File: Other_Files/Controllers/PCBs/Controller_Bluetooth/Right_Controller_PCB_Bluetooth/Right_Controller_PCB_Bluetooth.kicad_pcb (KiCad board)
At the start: 2 copper layers, 53 x 102 mm, 13 parts, among them X1 SW_Push, Y1 SW_Push

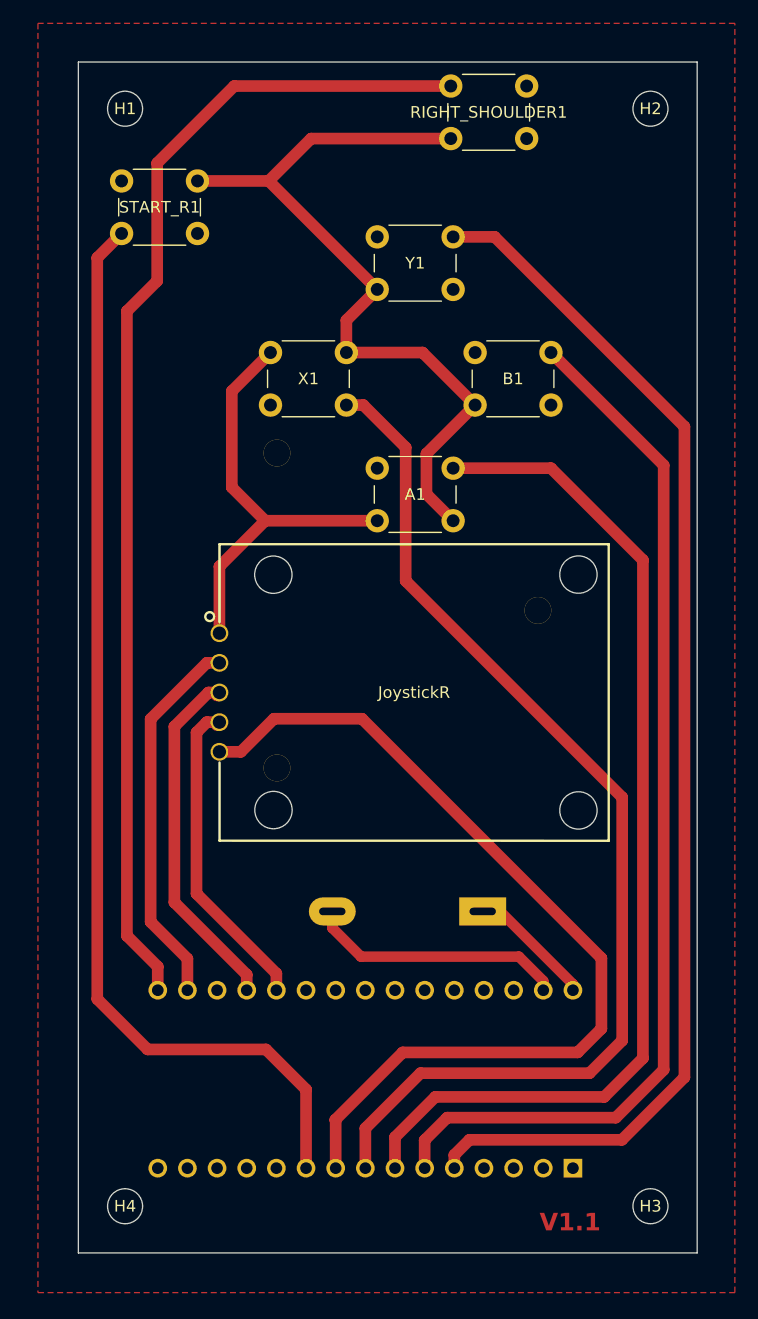
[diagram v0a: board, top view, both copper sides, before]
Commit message: Updated the Controllers' PCB to version 1.2
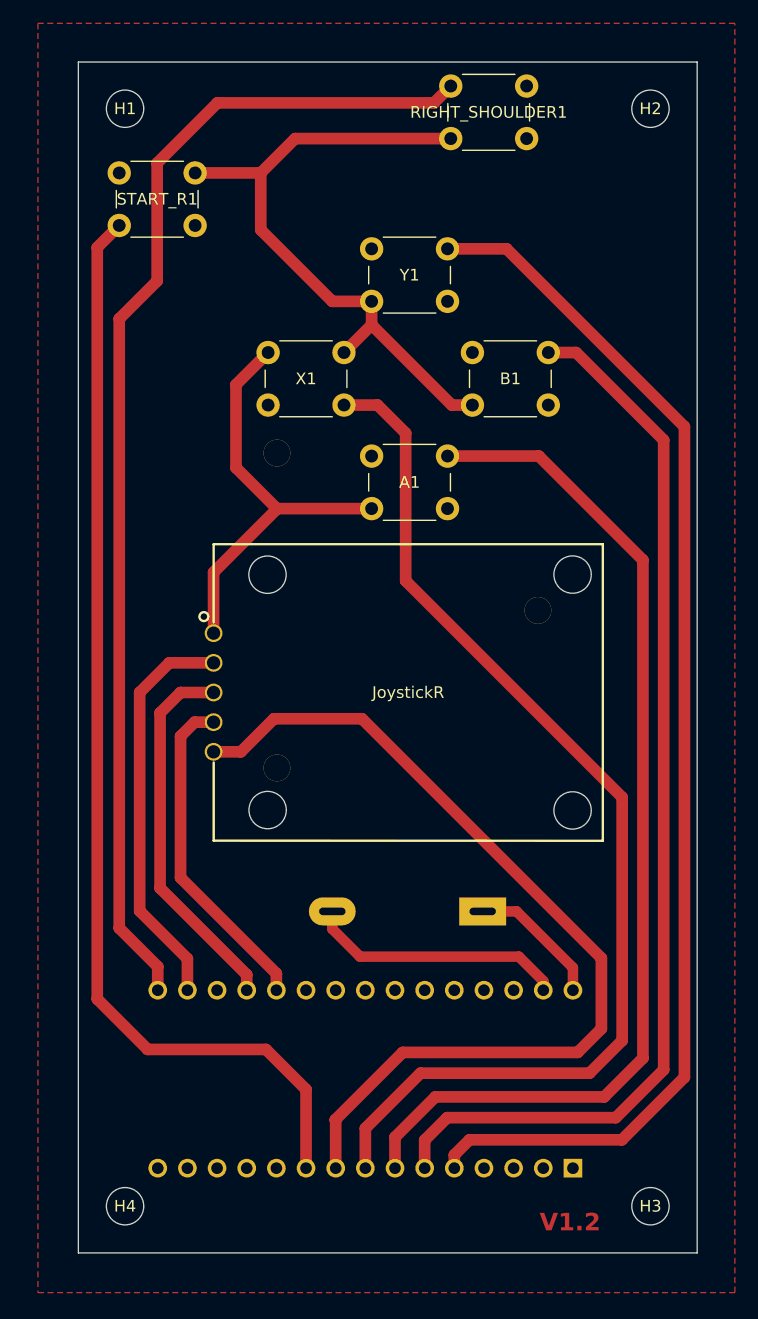
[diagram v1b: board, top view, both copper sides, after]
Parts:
- H1, H2, H3, H4: footprint MountingHole:MountingHole_3mm -> MountingHole:MountingHole_3.2mm_M3
- moved A1 1.14 mm to (142.1, 80.8)
- moved Y1 1.13 mm to (142.1, 63.0)
- moved START_R1 0.72 mm to (127.0, 61.0)
- moved JoystickR1 0.50 mm to (145.2, 101.0)
- moved B1 0.23 mm to (150.8, 71.9)
- moved X1 0.20 mm to (133.2, 71.9)
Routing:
- net GND: track 128.5 -> 116.3 mm
- net +3.3V: track 32.4 -> 34.6 mm
- net /Analog_X_R: track 30.5 -> 32.1 mm
- net /B: track 90.8 -> 92.3 mm
- net /Analog_Y_R: track 27.5 -> 28.5 mm
- net /X: track 93.6 -> 94.5 mm
- net /A: track 88.9 -> 89.8 mm
- net +9V: track 10.8 -> 11.7 mm
- net /START_R: track 94.3 -> 94.9 mm
- net /SEL_JOY_R: track 78.6 -> 79.1 mm
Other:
- board text added: "V1.2"
- board text removed: "V1.1"

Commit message: corrected previous commit
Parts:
- moved A1 0.12 mm to (142.0, 80.8)
- moved Y1 0.12 mm to (142.0, 63.0)
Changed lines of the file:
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@@
 	(footprint "Button_Switch_THT:SW_PUSH_6mm"
 		(layer "F.Cu")
-		(at 142.118 80.75)
+		(at 142 80.75)
 		(descr "Generic 6mm SW tactile push button")
 		(tags "tact sw push 6mm")
@@
 	(footprint "Button_Switch_THT:SW_PUSH_6mm"
 		(layer "F.Cu")
-		(at 142.118 63)
+		(at 142 63)
 		(descr "Generic 6mm SW tactile push button")
 		(tags "tact sw push 6mm")
@@
 	)
 	(segment
-		(start 132.622 56.5)
-		(end 132.622 61.372)
-		(width 1)
-		(layer "F.Cu")
-		(net 2)
-	)
-	(segment
-		(start 142.118 85.25)
-		(end 134.038 85.25)
-		(width 1)
-		(layer "F.Cu")
-		(net 2)
-	)
-	(segment
 		(start 128.5 95.85675)
 		(end 128.43675 95.92)
@@
 	)
 	(segment
-		(start 154.736258 123.625)
-		(end 156.82 125.708742)
-		(width 0.9)
+		(start 132.622 56.5)
+		(end 132.622 61.372)
+		(width 1)
 		(layer "F.Cu")
 		(net 2)
 	)
 	(segment
-		(start 134 85.25)
-		(end 130.5 81.75)
+		(start 139.75 71.882)
+		(end 142 71.882)
 		(width 1)
 		(layer "F.Cu")
@@
 	)
 	(segment
-		(start 142.118 67.5)
-		(end 142.118 69.514)
-		(width 1)
+		(start 154.736258 123.625)
+		(end 156.82 125.708742)
+		(width 0.9)
 		(layer "F.Cu")
 		(net 2)
 	)
 	(segment
-		(start 148.986 76.382)
-		(end 142.118 69.514)
+		(start 134 85.25)
+		(end 130.5 81.75)
 		(width 1)
 		(layer "F.Cu")
@@
 	)
 	(segment
+		(start 142 71.882)
+		(end 146.25 71.882)
+		(width 1)
+		(layer "F.Cu")
+		(net 2)
+	)
+	(segment
 		(start 130.5 74.632)
 		(end 133.25 71.882)
@@
 	)
 	(segment
-		(start 142.118 69.514)
-		(end 139.75 71.882)
+		(start 142 67.5)
+		(end 142.118 67.618)
 		(width 1)
 		(layer "F.Cu")
@@
 	)
 	(segment
-		(start 138.75 67.5)
-		(end 142.118 67.5)
+		(start 142 85.25)
+		(end 134.038 85.25)
 		(width 1)
 		(layer "F.Cu")
@@
 	)
 	(segment
-		(start 150.75 76.382)
-		(end 148.986 76.382)
+		(start 142 67.5)
+		(end 138.75 67.5)
 		(width 1)
 		(layer "F.Cu")
@@
 	)
 	(segment
+		(start 142 67.5)
+		(end 142 71.882)
+		(width 1)
+		(layer "F.Cu")
+		(net 2)
+	)
+	(segment
+		(start 146.25 71.882)
+		(end 150.75 76.382)
+		(width 1)
+		(layer "F.Cu")
+		(net 2)
+	)
+	(segment
 		(start 162.039236 135.636)
 		(end 147.574 135.636)
@@
 	)
 	(segment
+		(start 148.5 80.75)
+		(end 156.442 80.75)
+		(width 1)
+		(layer "F.Cu")
+		(net 5)
+	)
+	(segment
 		(start 156.442 80.75)
 		(end 165.354 89.662)
@@
 	)
 	(segment
-		(start 148.618 80.75)
-		(end 156.442 80.75)
-		(width 1)
-		(layer "F.Cu")
-		(net 5)
-	)
-	(segment
 		(start 157.25 71.882)
 		(end 159.632 71.882)
@@
 	)
 	(segment
-		(start 148.618 63)
-		(end 153.678 63)
+		(start 153.678 63)
+		(end 148.5 63)
 		(width 1)
 		(layer "F.Cu")

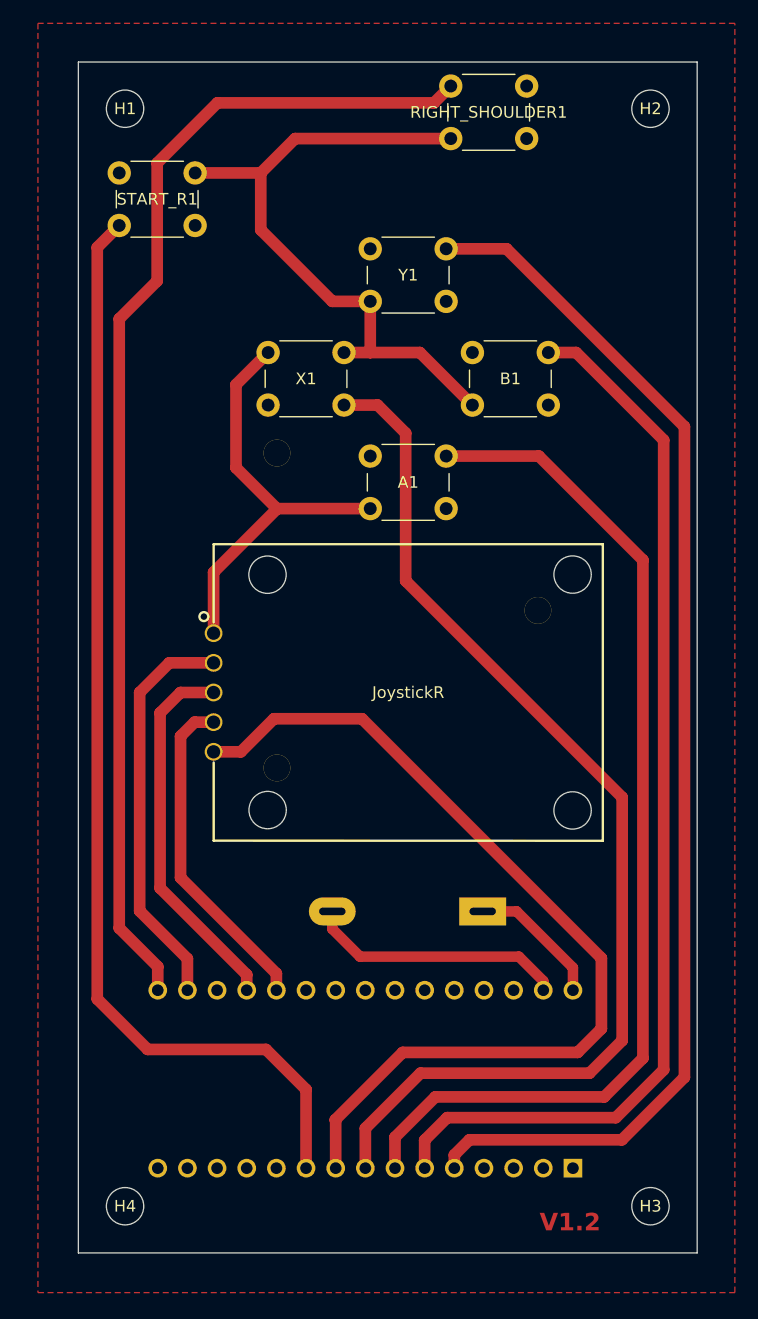
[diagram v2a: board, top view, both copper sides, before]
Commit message: Updated Bluetooth Controllers' PCBs
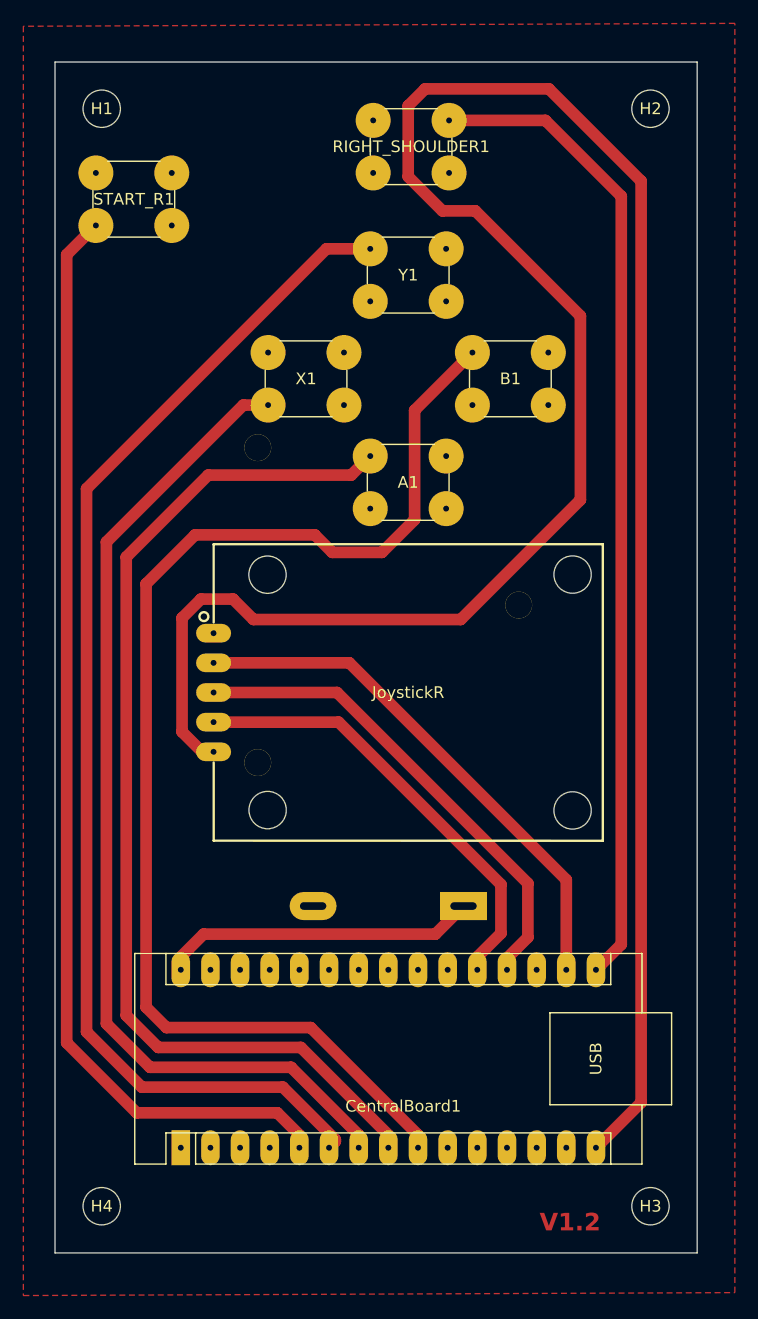
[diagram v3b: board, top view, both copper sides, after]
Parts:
- CentralBoard1: moved to F.Cu
- moved CentralBoard1 33.6 mm to (125.8, 140.0)
- moved RIGHT_SHOULDER1 7.27 mm to (142.2, 52.0)
- moved H1 2.00 mm to (119.0, 51.0)
- moved H4 2.00 mm to (119.0, 145.0)
- moved START_R1 2.00 mm to (125.0, 61.0)
- moved BAT9V1 1.71 mm to (150.0, 119.3)
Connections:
- CentralBoard1 pad 10: /START_R -> unconnected-(CentralBoard1-D7-Pad10)
- CentralBoard1 pad 15: unconnected-(CentralBoard1-D12-Pad15) -> /SEL_JOY_R
- CentralBoard1 pad 5: /Y -> /START_R
- CentralBoard1 pad 6: /B -> /Y
- CentralBoard1 pad 7: /A -> /X
- CentralBoard1 pad 8: /X -> /A
- CentralBoard1 pad 9: /SEL_JOY_R -> /B
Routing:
- net /SEL_JOY_R: track 79.1 -> 202.6 mm
- net GND: track 116.6 -> 0.00 mm
- net /RIGHT_SHOULDER: track 101.4 -> 84.6 mm
- net /B: track 92.3 -> 108.1 mm
- net +9V: track 11.7 -> 27.1 mm
- net +3.3V: track 34.6 -> 45.6 mm
- net /Analog_Y_R: track 28.5 -> 38.5 mm
- net /Analog_X_R: track 32.1 -> 41.8 mm
- net /X: track 94.5 -> 86.6 mm
- net /A: track 89.9 -> 91.5 mm
- net /Y: track 106.0 -> 105.4 mm
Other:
- board size 53 x 102 mm -> 55 x 102 mm
